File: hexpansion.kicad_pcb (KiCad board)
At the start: 2 copper layers, 32 x 36.6 mm, 7 parts, among them J1 Nodule-Connector, J2 Conn_02x10_Odd_Even

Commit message: extract out hexpansion parts to custom library
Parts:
- J1: value Nodule-Connector -> Hexpansion-Connector; footprint tildagon:hexpansion-edge-connector -> parts:hexpansion-edge-connector
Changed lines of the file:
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@@
 	(net 14 "Net-(D1-A)")
 	(net 15 "/HEXP_DET")
-	(footprint "tildagon:hexpansion-edge-connector"
+	(footprint "parts:hexpansion-edge-connector"
 		(layer "F.Cu")
 		(at 98.25 100)
@@
 			)
 		)
-		(property "Value" "Nodule-Connector"
+		(property "Value" "Hexpansion-Connector"
 			(at 0 1 0)
 			(unlocked yes)
@@
 			)
 		)
-		(property "Footprint" ""
+		(property "Footprint" "parts:hexpansion-edge-connector"
 			(at 0 0 0)
 			(unlocked yes)
@@
 			)
 		)
+		(sheetname "Root")
 		(sheetfile "hexpansion.kicad_sch")
 		(attr exclude_from_pos_files exclude_from_bom)
@@
 			(layer "F.CrtYd")
 		)
+		(fp_text user "1"
+			(at 5.2 3.05 90)
+			(unlocked yes)
+			(layer "B.SilkS")
+			(effects
+				(font
+					(size 0.8 0.8)
+					(thickness 0.2)
+					(bold yes)
+				)
+				(justify left bottom mirror)
+			)
+		)
 		(fp_text user "BOTTOM!"
 			(at 5.7 -4.3 90)
@@
 					(size 1 1)
 					(thickness 0.25)
-					(bold yes)
-				)
-				(justify left bottom mirror)
-			)
-		)
-		(fp_text user "1"
-			(at 5.2 3.05 90)
-			(unlocked yes)
-			(layer "B.SilkS")
-			(effects
-				(font
-					(size 0.8 0.8)
-					(thickness 0.2)
 					(bold yes)
 				)
@@
 			)
 		)
-		(property "Footprint" ""
+		(property "Footprint" "LED_SMD:LED_0805_2012Metric"
 			(at 0 0 -90)
 			(unlocked yes)
@@
 			)
 		)
-		(property "Description" "Light emitting diode"
+		(property "Description" ""
 			(at 0 0 -90)
 			(unlocked yes)
@@
 			)
 		)
+		(property ki_fp_filters "LED* LED_SMD:* LED_THT:*")
+		(sheetname "Root")
 		(sheetfile "hexpansion.kicad_sch")
 		(attr smd)
@@
 			)
 		)
-		(property "Footprint" ""
+		(property "Footprint" "MountingHole:MountingHole_2.2mm_M2_Pad_Via"
 			(at 0 0 0)
 			(unlocked yes)
@@
 			)
 		)
-		(property "Description" "Mounting Hole with connection"
+		(property "Description" ""
 			(at 0 0 0)
 			(unlocked yes)
@@
 			)
 		)
+		(property ki_fp_filters "MountingHole*Pad*")
+		(sheetname "Root")
 		(sheetfile "hexpansion.kicad_sch")
 		(attr exclude_from_pos_files)
@@
 			)
 		)
-		(property "Footprint" ""
+		(property "Footprint" "Connector_PinHeader_2.54mm:PinHeader_2x10_P2.54mm_Vertical"
 			(at 0 0 180)
 			(unlocked yes)
@@
 			)
 		)
-		(property "Description" "Generic connector, double row, 02x10, odd/even pin numbering scheme (row 1 odd numbers, row 2 even numbers), script generated (kicad-library-utils/schlib/autogen/connector/)"
+		(property "Description" ""
 			(at 0 0 180)
 			(unlocked yes)
@@
 			)
 		)
+		(property ki_fp_filters "Connector*:*_2x??_*")
+		(sheetname "Root")
 		(sheetfile "hexpansion.kicad_sch")
 		(attr through_hole)
@@
 			)
 		)
-		(property "Footprint" ""
+		(property "Footprint" "Jumper:SolderJumper-2_P1.3mm_Bridged_RoundedPad1.0x1.5mm"
 			(at 0 0 90)
 			(unlocked yes)
@@
 			)
 		)
-		(property "Description" "Solder Jumper, 2-pole, closed/bridged"
+		(property "Description" ""
 			(at 0 0 90)
 			(unlocked yes)
@@
 			)
 		)
+		(property ki_fp_filters "SolderJumper*Bridged*")
+		(sheetname "Root")
 		(sheetfile "hexpansion.kicad_sch")
 		(attr exclude_from_pos_files)
@@
 			)
 		)
-		(property "Footprint" ""
+		(property "Footprint" "Resistor_SMD:R_0603_1608Metric"
 			(at 0 0 90)
 			(unlocked yes)
@@
 			)
 		)
-		(property "Description" "Resistor"
+		(property "Description" ""
 			(at 0 0 90)
 			(unlocked yes)
@@
 			)
 		)
+		(property ki_fp_filters "R_*")
+		(sheetname "Root")
 		(sheetfile "hexpansion.kicad_sch")
 		(attr smd)
@@
 			)
 		)
-		(property "Footprint" ""
+		(property "Footprint" "MountingHole:MountingHole_2.2mm_M2_Pad_Via"
 			(at 0 0 0)
 			(unlocked yes)
@@
 			)
 		)
-		(property "Description" "Mounting Hole with connection"
+		(property "Description" ""
 			(at 0 0 0)
 			(unlocked yes)
@@
 			)
 		)
+		(property ki_fp_filters "MountingHole*Pad*")
+		(sheetname "Root")
 		(sheetfile "hexpansion.kicad_sch")
 		(attr exclude_from_pos_files)

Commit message: rough everything
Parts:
- removed D1: LED, LED_SMD:LED_0805_2012Metric
- added C1: 10 uF, Capacitor_SMD:C_0603_1608Metric, F.Cu at (115.2, 99.0)
- added C10: 10 uF, Capacitor_SMD:C_0603_1608Metric, F.Cu at (108.8, 102.5)
- added C11: 0.1 uF, Capacitor_SMD:C_0402_1005Metric, F.Cu at (110.0, 102.0)
- added C12: 0.1 uF, Capacitor_SMD:C_0402_1005Metric, F.Cu at (111.0, 102.0)
- added C13: 47 uF, Capacitor_SMD:C_1206_3216Metric, F.Cu at (119.2, 92.2)
- added C14: 47 uF, Capacitor_SMD:C_1206_3216Metric, F.Cu at (119.2, 96.2)
- added C15: 1 uF, Capacitor_SMD:C_1206_3216Metric, F.Cu at (119.2, 101.0)
- added C16: 1 uF, Capacitor_SMD:C_1206_3216Metric, F.Cu at (119.2, 105.0)
- added C17: 1 uF, Capacitor_SMD:C_1206_3216Metric, F.Cu at (120.0, 87.0)
- added C18: 1 uF, Capacitor_SMD:C_1206_3216Metric, F.Cu at (117.5, 87.0)
- added C19: 1 uF, Capacitor_SMD:C_1206_3216Metric, F.Cu at (117.5, 114.0)
- added C2: 10 uF, Capacitor_SMD:C_0603_1608Metric, F.Cu at (109.0, 92.0)
- added C20: 1 uF, Capacitor_SMD:C_1206_3216Metric, F.Cu at (120.0, 114.0)
- added C21: 0.1 uF, Capacitor_SMD:C_0402_1005Metric, F.Cu at (110.5, 104.2)
- added C3: 0.1 uF, Capacitor_SMD:C_0402_1005Metric, F.Cu at (108.5, 94.0)
- added C4: 10 uF, Capacitor_SMD:C_0603_1608Metric, F.Cu at (107.0, 92.0)
- added C5: 0.1 uF, Capacitor_SMD:C_0402_1005Metric, F.Cu at (106.5, 94.0)
- added C6: 10 uF, Capacitor_SMD:C_0603_1608Metric, F.Cu at (110.8, 92.0)
- added C7: 0.1 uF, Capacitor_SMD:C_0402_1005Metric, F.Cu at (110.5, 94.0)
- added C8: 10 uF, Capacitor_SMD:C_0603_1608Metric, F.Cu at (112.2, 92.0)
- added C9: 0.1 uF, Capacitor_SMD:C_0402_1005Metric, F.Cu at (112.5, 94.0)
- added J3: AudioJack4, Connector_Audio:Jack_3.5mm_PJ320D_Horizontal, F.Cu at (128.0, 100.0)
- added J4: AudioJack4, Connector_Audio:Jack_3.5mm_PJ320D_Horizontal, F.Cu at (128.0, 111.0)
- added JP2: ADDR_LSB0, Jumper:SolderJumper-3_P1.3mm_Bridged12_RoundedPad1.0x1.5mm, B.Cu at (103.0, 92.5)
- added R2: 10, Resistor_SMD:R_0603_1608Metric, F.Cu at (120.0, 94.2)
- added R3: 10, Resistor_SMD:R_0603_1608Metric, F.Cu at (120.0, 103.0)
- added R4: 10, Resistor_SMD:R_0603_1608Metric, F.Cu at (120.0, 99.0)
- added R5: 10k, Resistor_SMD:R_0402_1005Metric, F.Cu at (106.0, 99.0)
- added R6: 10k, Resistor_SMD:R_0402_1005Metric, F.Cu at (106.0, 100.0)
- added R7: 10k, Resistor_SMD:R_0402_1005Metric, F.Cu at (114.5, 107.0)
- added R8: 10k, Resistor_SMD:R_0402_1005Metric, F.Cu at (108.0, 109.8)
- added TP1: TestPoint, TestPoint:TestPoint_Pad_2.0x2.0mm, F.Cu at (119.0, 83.0)
- added TP2: SCL, TestPoint:TestPoint_Pad_2.0x2.0mm, B.Cu at (109.5, 102.5)
- added TP3: SDA, TestPoint:TestPoint_Pad_2.0x2.0mm, B.Cu at (106.5, 102.5)
- added TP4: ASDOUT, TestPoint:TestPoint_Pad_1.0x1.0mm, B.Cu at (112.5, 106.0)
- added TP5: DSDIN, TestPoint:TestPoint_Pad_1.0x1.0mm, B.Cu at (108.5, 106.0)
- added U1: ~, parts:QFN-28-1EP_4x4mm_P0.45mm_EP2.6x2.6mm, F.Cu at (111.0, 98.0)
- added U2: 74LVC1G125, Package_TO_SOT_SMD:SOT-23-5, F.Cu at (112.0, 107.0)
- added U3: 74LVC1G125, Package_TO_SOT_SMD:SOT-23-5, F.Cu at (108.0, 107.0)
- J2: value Conn_02x10_Odd_Even -> AudioJack4; footprint Connector_PinHeader_2.54mm:PinHeader_2x10_P2.54mm_Vertical -> Connector_Audio:Jack_3.5mm_PJ320D_Horizontal
- JP1: moved to B.Cu
- R1: value R -> 10
- moved JP1 23.7 mm to (107.0, 96.5)
- moved J2 22.7 mm to (128.0, 89.0)
- moved R1 17.9 mm to (120.0, 90.2), turned to 0 degrees
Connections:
- H1 pad 1: /GND -> GND
- H2 pad 1: /GND -> GND
- J1 pad 1: /GND -> GND
- J1 pad 10: /GND -> GND
- J1 pad 11: /GND -> GND
- J1 pad 12: /HS_F -> /MCLK
- J1 pad 13: /HS_G -> /SCLK
- J1 pad 14: /GND -> GND
- J1 pad 15: /3V3 -> +3.3V
- J1 pad 16: /3V3 -> +3.3V
- J1 pad 17: /GND -> GND
- J1 pad 18: /HS_H -> /LRCLK
- J1 pad 19: /HS_I -> /I2S_DATA_SHARED
- J1 pad 2: /LS_A -> /~{MIC_EN}
- J1 pad 20: /GND -> GND
- J1 pad 3: /LS_B -> /~{OUT_EN}
- J1 pad 7: /LS_C -> unconnected-(J1-LS_C-Pad7)
- J1 pad 8: /LS_D -> unconnected-(J1-LS_D-Pad8)
- J1 pad 9: /LS_E -> unconnected-(J1-LS_E-Pad9)
- JP1 pad 2: /GND -> GND
- R1 pad 1: /3V3 -> Net-(C13-Pad2)
- R1 pad 2: Net-(D1-A) -> /HP_L
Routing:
- net /GND: track 207.4 -> 0.00 mm, vias 2 -> 0
- net /3V3: track 56.5 -> 0.00 mm, vias 1 -> 0
- net /HEXP_DET: track 32.8 -> 0.00 mm
- net /LS_E: track 27.2 -> 0.00 mm
- net /LS_D: track 26.1 -> 0.00 mm
- net /LS_A: track 25.9 -> 0.00 mm
- net /LS_C: track 25.5 -> 0.00 mm
- net /LS_B: track 25.2 -> 0.00 mm
- net /SDA: track 24.5 -> 0.00 mm
- net /SCL: track 24.0 -> 0.00 mm
- net /HS_F: track 23.4 -> 0.00 mm
- net /HS_I: track 23.2 -> 0.00 mm
- net /HS_G: track 22.7 -> 0.00 mm
- net /HS_H: track 22.5 -> 0.00 mm
- net Net-(D1-A): track 1.64 -> 0.00 mm
- added copper zone on B.Cu, net GND
- added copper zone on F.Cu, net GND
- removed copper zone on B.Cu, net /GND
- removed copper zone on F.Cu, net /GND
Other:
- board size 32 x 36.6 mm -> 37 x 38 mm
- board text removed: "3V3"
- board text removed: "G"
- board text removed: "HS_F"
- board text removed: "HS_G"
- board text removed: "HS_H"
- board text removed: "HS_I"
- board text removed: "LS_A"
- board text removed: "LS_B"
- board text removed: "LS_C"
- board text removed: "LS_D"
- board text removed: "LS_E"
- board text removed: "ND"
- board text removed: "SCL"
- board text removed: "SDA"
- board text removed: "You may expand the hexpansion in this area"

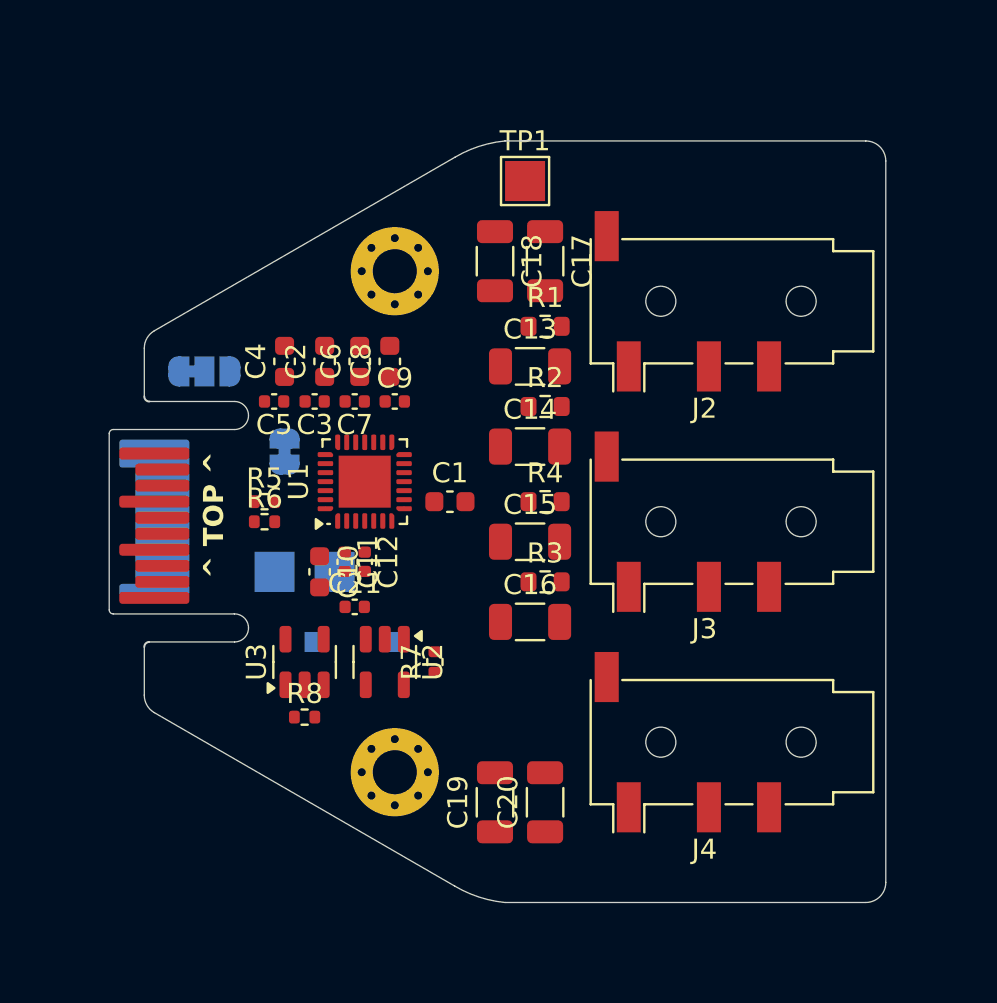
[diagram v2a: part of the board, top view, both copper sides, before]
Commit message: rough route
purposely ignore extra gnd
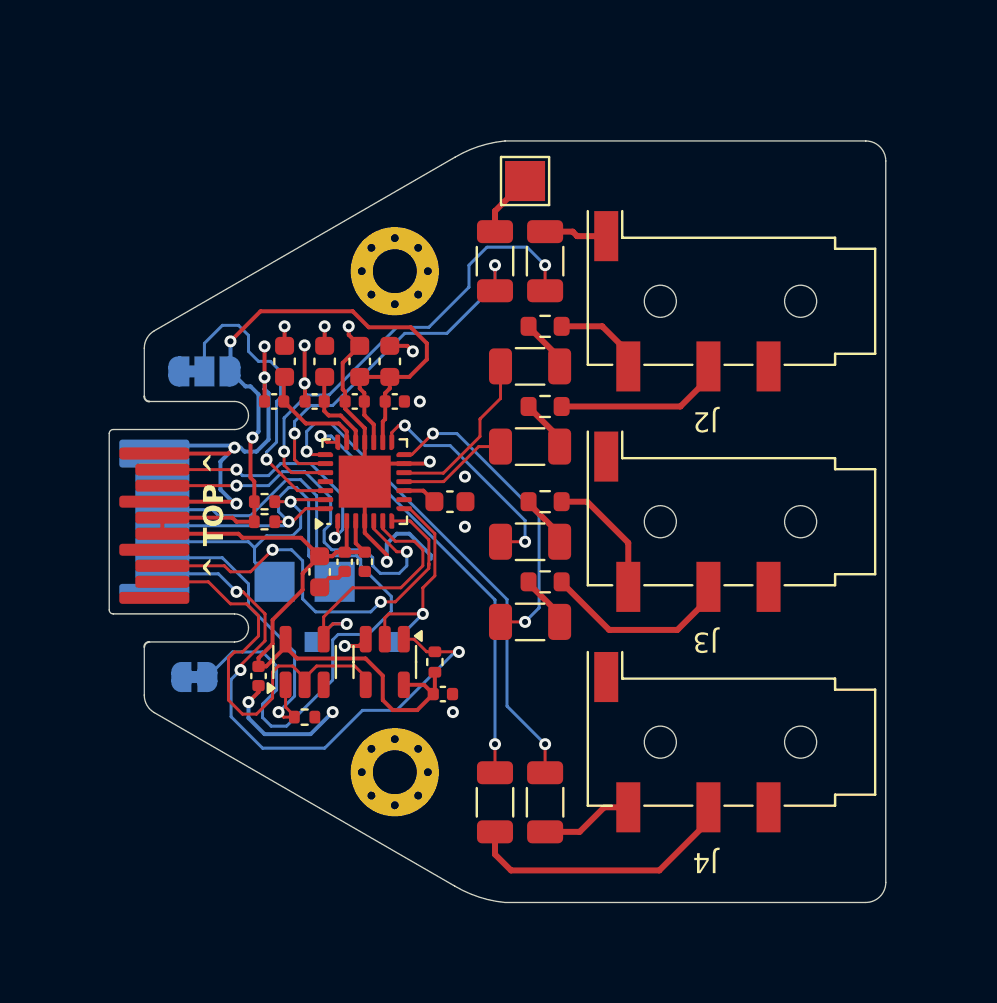
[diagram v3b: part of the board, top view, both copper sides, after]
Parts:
- added C22: 0.1 uF, Capacitor_SMD:C_0402_1005Metric, F.Cu at (114.9, 108.6)
- J2, J3, J4: footprint Connector_Audio:Jack_3.5mm_PJ320D_Horizontal -> Connector_Audio:Jack_3.5mm_KoreanHropartsElec_PJ-320D-4A_Horizontal
- moved JP1 12.1 mm to (102.5, 107.8), turned to 180 degrees
- moved C21 5.91 mm to (105.7, 107.7), turned to -90 degrees
- moved C19 2.50 mm to (120.0, 114.0)
- moved C20 2.50 mm to (117.5, 114.0)
- moved TP2 0.50 mm to (109.5, 103.0)
- moved TP3 0.50 mm to (106.5, 103.0)
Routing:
- net +3.3V: track 0.00 -> 73.4 mm, vias 0 -> 2
- net GND: track 0.00 -> 64.2 mm, vias 0 -> 19
- net /HEXP_DET: track 0.00 -> 34.4 mm
- net /~{MIC_EN}: track 0.00 -> 28.8 mm, vias 0 -> 3
- net Net-(U1-LIN2): track 0.00 -> 25.2 mm, vias 0 -> 2
- net Net-(U1-LIN1): track 0.00 -> 23.4 mm, vias 0 -> 2
- net Net-(U1-RIN2): track 0.00 -> 21.7 mm, vias 0 -> 2
- net /LRCLK: track 0.00 -> 20.9 mm, vias 0 -> 2
- net /I2S_DATA_SHARED: track 0.00 -> 20.9 mm
- net /SCLK: track 0.00 -> 20.0 mm, vias 0 -> 2
- net Net-(U1-RIN1): track 0.00 -> 18.6 mm, vias 0 -> 2
- net /SCL: track 0.00 -> 17.2 mm, vias 0 -> 1
- net Net-(U1-ROUT2): track 0.00 -> 15.7 mm, vias 0 -> 2
- net Net-(JP2-C): track 0.00 -> 15.3 mm, vias 0 -> 1
- net /~{OUT_EN}: track 0.00 -> 15.2 mm, vias 0 -> 1
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
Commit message: tweaks
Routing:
- net /LINEOUT_L: track 6.37 -> 5.63 mm

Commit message: more small tweaks
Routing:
- net Net-(U1-ROUT2): track 15.7 -> 16.3 mm

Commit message: metadata
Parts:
- TP1: value TestPoint -> MIC_R

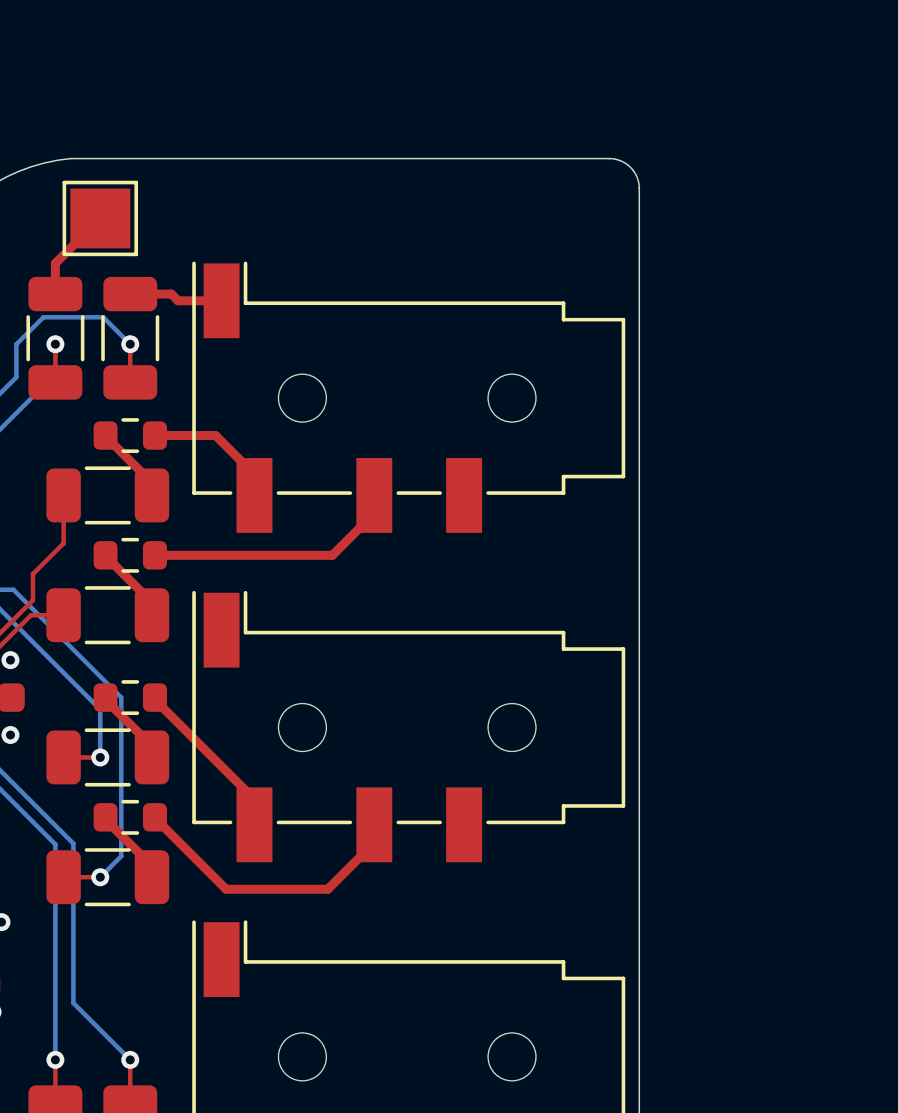
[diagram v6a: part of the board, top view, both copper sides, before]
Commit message: doodles, fab layer cleanup
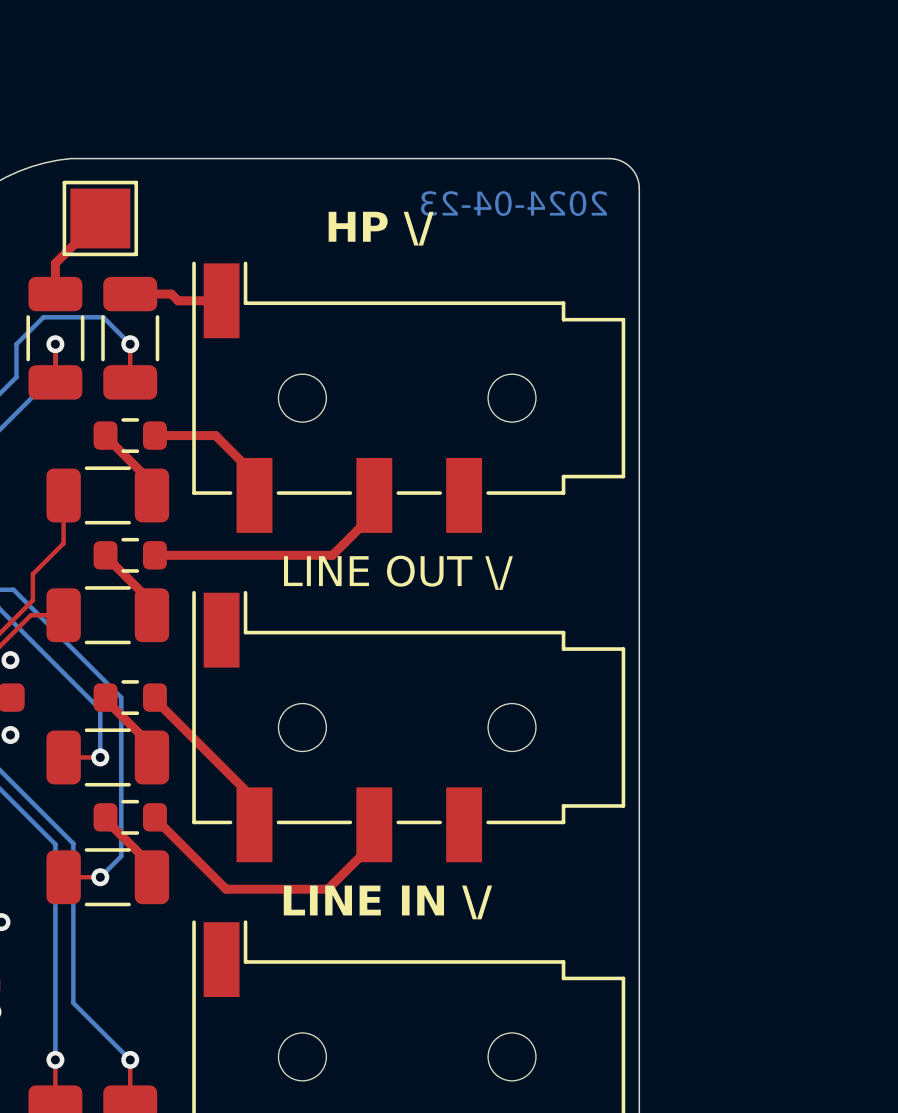
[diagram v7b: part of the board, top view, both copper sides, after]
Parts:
- U1: value ~ -> ES8388
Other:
- board text added: "(x4)"
- board text added: "2024-04-23"
- board text added: "ADDR[0]"
- board text added: "HP \/"
- board text added: "LINE IN \/"
- board text added: "LINE OUT \/"
- board text added: "They removed the headphone jack! Design by R"
